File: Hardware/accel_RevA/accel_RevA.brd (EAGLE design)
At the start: 100 x 80 mm, 12 parts, among them U1 MMA8452Q

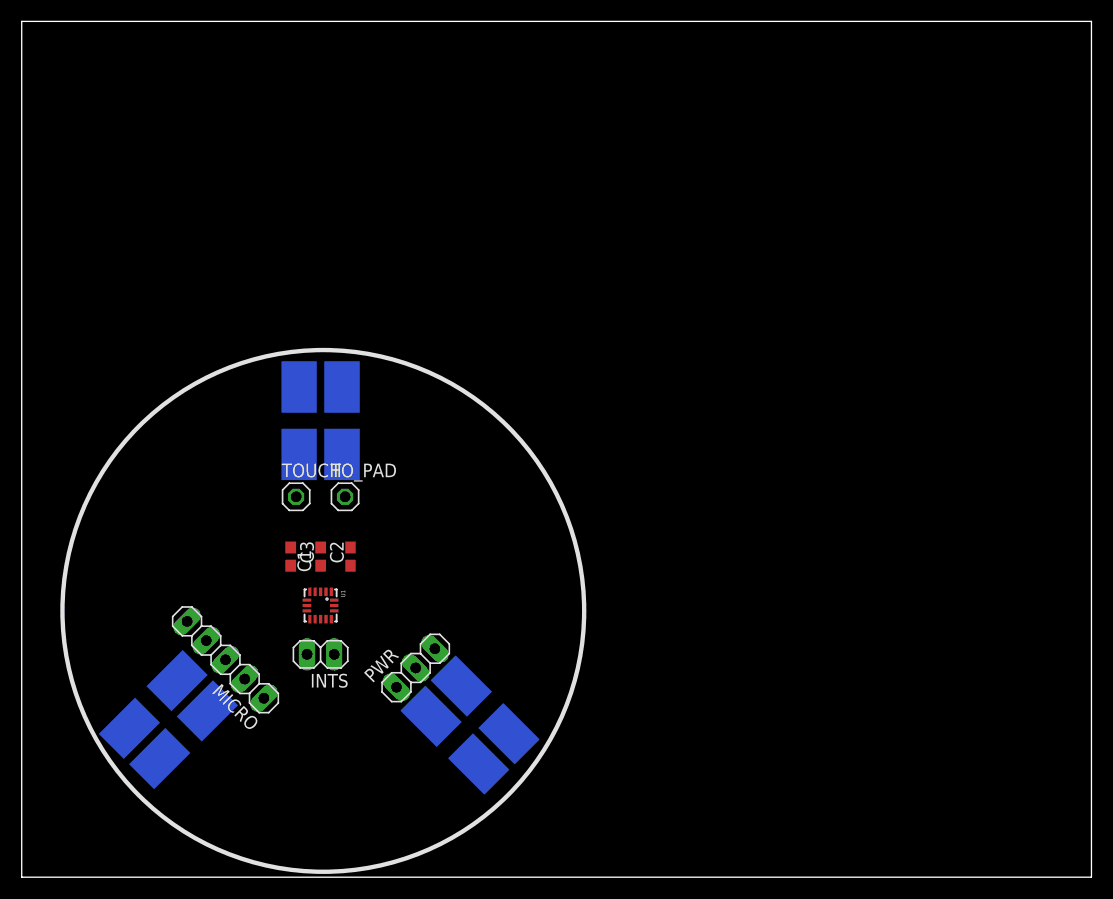
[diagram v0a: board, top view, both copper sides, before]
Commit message: Update of revA of accel board
Completed routing of board!! No rats nest left, passes DRC and ERC.
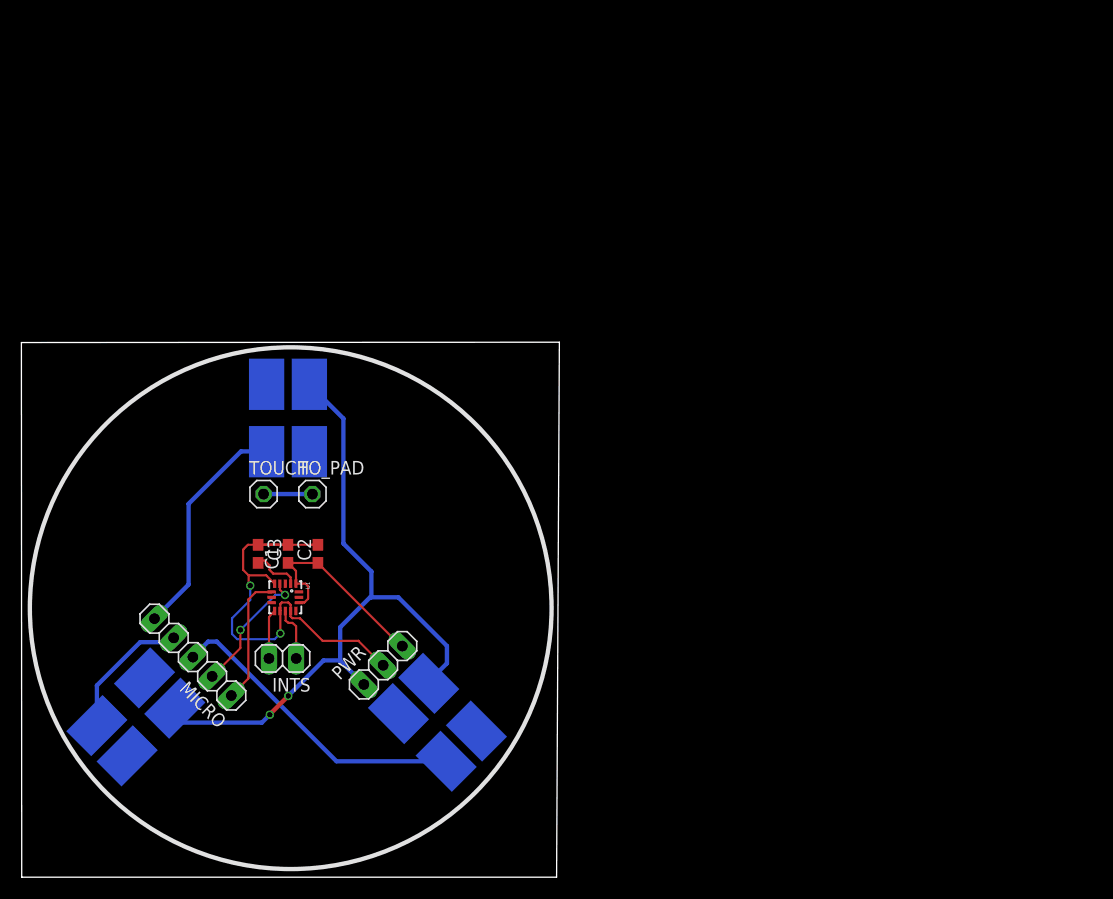
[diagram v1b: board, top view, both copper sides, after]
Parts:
- moved INTS 3.58 mm to (24.4, 20.4)
- moved U1 3.39 mm to (24.6, 26.2)
- moved LED3 3.06 mm to (24.9, 42.9)
- moved C1 3.06 mm to (22.1, 30.2)
- moved C2 3.06 mm to (27.7, 30.2)
- moved C3 3.06 mm to (24.9, 30.2)
- moved MICRO 3.06 mm to (16.0, 20.6)
- moved PWR 3.06 mm to (33.8, 19.8)
- moved LED2 3.06 mm to (10.7, 15.0)
- moved TOUCH 3.06 mm to (22.6, 35.8)
- moved TO_PAD 3.06 mm to (27.2, 35.8)
- moved LED1 3.06 mm to (38.9, 14.5)
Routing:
- net VDD: track 0.00 -> 65.1 mm, vias 0 -> 2
- net GND: track 0.00 -> 42.1 mm, vias 0 -> 2
- net LED1: track 0.00 -> 28.9 mm
- net LED3: track 0.00 -> 21.4 mm
- net VCC: track 0.00 -> 19.6 mm
- net LED2: track 0.00 -> 12.8 mm
- net SCL: track 0.00 -> 12.2 mm, vias 0 -> 2
- net SDA: track 0.00 -> 12.1 mm
- net N$1: track 0.00 -> 5.11 mm
- net N$2: track 0.00 -> 4.64 mm
- net N$3: track 0.00 -> 4.62 mm
- net TOUCH: track 0.00 -> 4.57 mm
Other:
- board size 100 x 80 mm -> 50.3 x 50 mm

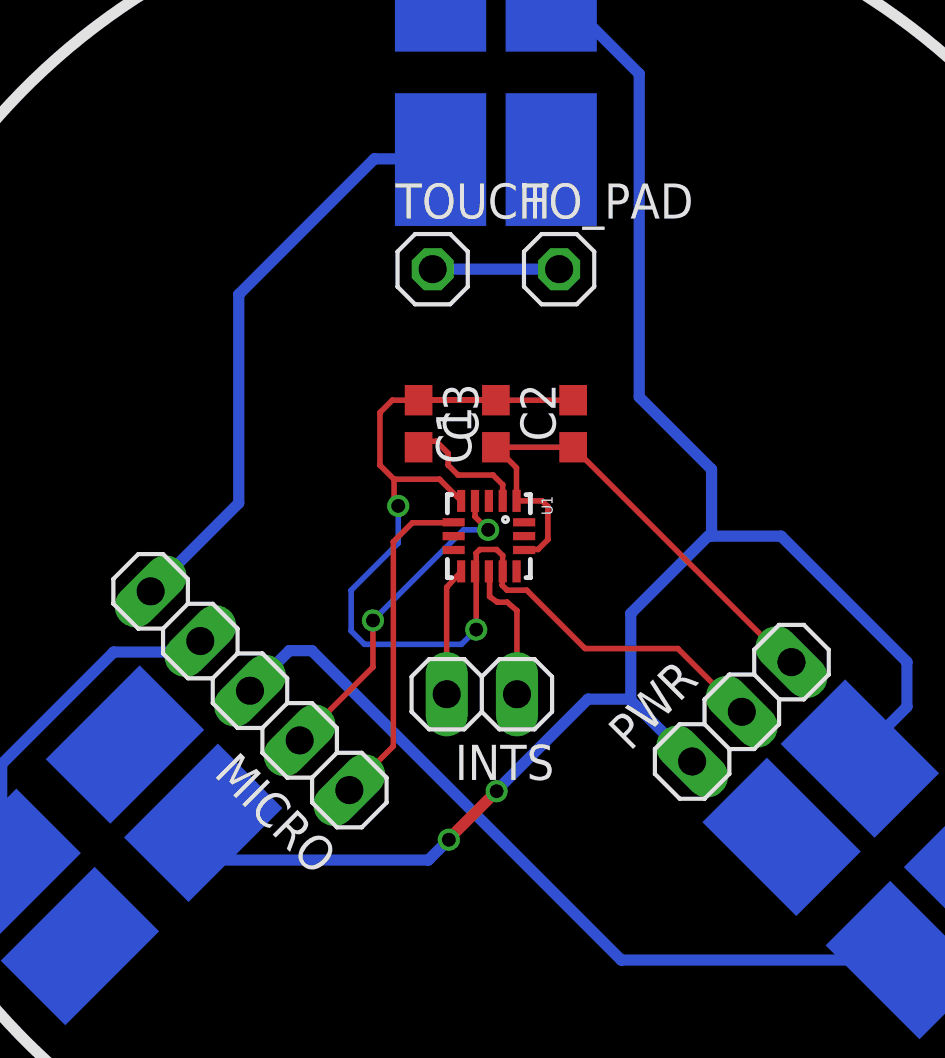
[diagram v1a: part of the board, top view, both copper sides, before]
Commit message: Added names to stuff on board
Just the names and stuff, not really much. Just needs some legit
artwork.
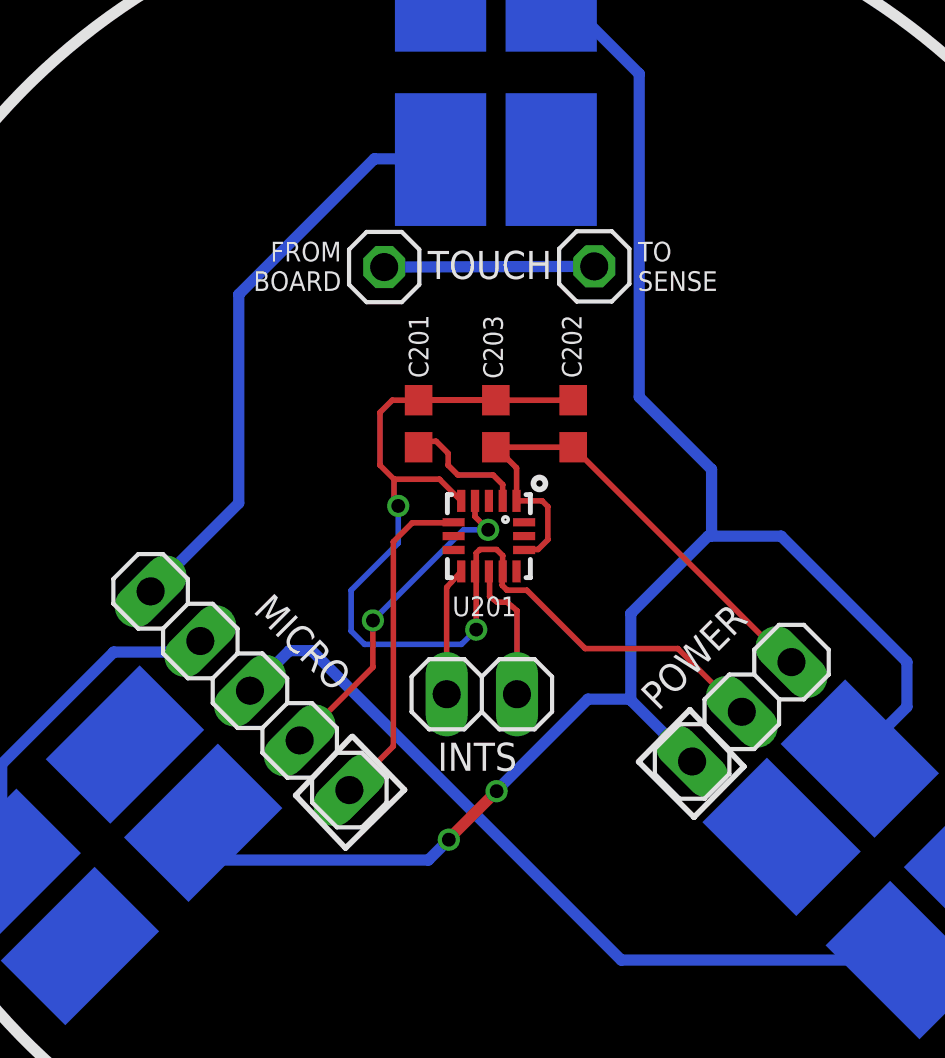
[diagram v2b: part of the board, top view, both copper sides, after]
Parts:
- moved TOUCH 1.75 mm to (20.9, 35.9)
- moved TO_PAD 1.27 mm to (28.4, 35.9)
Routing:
- net TOUCH: track 4.57 -> 7.59 mm
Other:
- board text added: "C201"
- board text added: "C202"
- board text added: "C203"
- board text added: "FROM BOARD"
- board text added: "INTS"
- board text added: "MICRO"
- board text added: "POWER"
- board text added: "TO SENSE"
- board text added: "TOUCH"
- board text added: "U201"
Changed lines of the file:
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@@
 <circle x="25.146" y="25.146" radius="24.385321875" width="0.4064" layer="21"/>
 <circle x="25.146" y="25.146" radius="24.385321875" width="0.4064" layer="22"/>
+<text x="22.4536" y="31.877" size="0.7112" layer="21" ratio="10" rot="R90">C201</text>
+<text x="25.146" y="31.8516" size="0.7112" layer="21" ratio="10" rot="R90">C203</text>
+<text x="27.9908" y="31.877" size="0.7112" layer="21" ratio="10" rot="R90">C202</text>
+<circle x="26.4668" y="28.067" radius="0.217015625" width="0.2032" layer="21"/>
+<text x="23.3172" y="23.2664" size="0.7112" layer="21" ratio="10">U201</text>
+<text x="22.7838" y="17.6784" size="1.016" layer="21" ratio="16">INTS</text>
+<text x="16.0782" y="23.4442" size="1.016" layer="21" ratio="16" rot="R315">MICRO</text>
+<text x="30.7594" y="19.812" size="1.016" layer="21" ratio="16" rot="R45">POWER</text>
+<text x="22.4282" y="35.4584" size="1.016" layer="21" ratio="19">TOUCH</text>
+<wire x1="19.7104" y1="18.923" x2="21.59" y2="16.9926" width="0.2032" layer="21"/>
+<wire x1="21.59" y1="16.9926" x2="19.4564" y2="14.8844" width="0.2032" layer="21"/>
+<wire x1="19.4564" y1="14.8844" x2="17.653" y2="16.7894" width="0.2032" layer="21"/>
+<wire x1="17.653" y1="16.7894" x2="19.6596" y2="18.8976" width="0.2032" layer="21"/>
+<wire x1="30.0482" y1="18.0086" x2="31.9024" y2="19.8882" width="0.2032" layer="21"/>
+<wire x1="31.9024" y1="19.8882" x2="33.8582" y2="17.8308" width="0.2032" layer="21"/>
+<wire x1="33.8582" y1="17.8308" x2="32.0548" y2="16.002" width="0.2032" layer="21"/>
+<wire x1="32.0548" y1="16.002" x2="30.0736" y2="17.9832" width="0.2032" layer="21"/>
+<text x="30.0228" y="35.0266" size="0.7112" layer="21">TO
+SENSE</text>
+<text x="19.304" y="35.0266" size="0.7112" layer="21" align="bottom-right">FROM
+BOARD</text>
 </plain>
 <attributes>
@@
 </autorouter>
 <elements>
-<element name="U1" library="SparkFun-Sensors" package="QFN-16_0.5MM" value="MMA8452Q" x="24.638" y="26.162" rot="R270">
+<element name="U1" library="SparkFun-Sensors" package="QFN-16_0.5MM" value="MMA8452Q" x="24.638" y="26.162" smashed="yes" rot="R270">
 <attribute name="PROD_ID" value="IC-10769" x="-2.032" y="2.032" size="1.778" layer="27" rot="R270" display="off"/>
-</element>
-<element name="C1" library="eagle-ltspice" package="C0603" value="0.1u" x="22.098" y="30.226" rot="R270">
+<attribute name="VALUE" x="22.2746" y="27.6136" size="0.4064" layer="27" rot="R270"/>
+</element>
+<element name="C1" library="eagle-ltspice" package="C0603" value="0.1u" x="22.098" y="30.226" smashed="yes" rot="R270">
 <attribute name="SPICEMODEL" value="NONE" x="-9.652" y="13.716" size="1.778" layer="27" rot="R270" display="off"/>
 <attribute name="SPICEPREFIX" value="C" x="-9.652" y="13.716" size="1.778" layer="27" rot="R270" display="off"/>
-</element>
-<element name="C2" library="eagle-ltspice" package="C0603" value="0.1u" x="27.686" y="30.226" rot="R90">
+<attribute name="VALUE" x="20.193" y="30.861" size="1.27" layer="27" rot="R270"/>
+</element>
+<element name="C2" library="eagle-ltspice" package="C0603" value="0.1u" x="27.686" y="30.226" smashed="yes" rot="R90">
 <attribute name="SPICEMODEL" value="NONE" x="59.436" y="51.816" size="1.778" layer="27" rot="R90" display="off"/>
 <attribute name="SPICEPREFIX" value="C" x="59.436" y="51.816" size="1.778" layer="27" rot="R90" display="off"/>
-</element>
-<element name="PWR" library="pinhead" package="1X03" value="" x="33.782" y="19.812" rot="R45"/>
-<element name="MICRO" library="pinhead" package="1X05" value="" x="16.002" y="20.574" rot="R135"/>
-<element name="C3" library="eagle-ltspice" package="C0603" value="4.7u" x="24.892" y="30.226" rot="R90">
+<attribute name="VALUE" x="29.591" y="29.591" size="1.27" layer="27" rot="R90"/>
+</element>
+<element name="PWR" library="pinhead" package="1X03" value="" x="33.782" y="19.812" smashed="yes" rot="R45">
+<attribute name="VALUE" x="33.332984375" y="14.87285625" size="1.27" layer="27" rot="R45"/>
+</element>
+<element name="MICRO" library="pinhead" package="1X05" value="" x="16.002" y="20.574" smashed="yes" rot="R135">
+<attribute name="VALUE" x="22.737190625" y="18.328934375" size="1.27" layer="27" rot="R135"/>
+</element>
+<element name="C3" library="eagle-ltspice" package="C0603" value="4.7u" x="24.892" y="30.226" smashed="yes" rot="R90">
 <attribute name="SPICEMODEL" value="NONE" x="56.642" y="56.896" size="1.778" layer="27" rot="R90" display="off"/>
 <attribute name="SPICEPREFIX" value="C" x="56.642" y="56.896" size="1.778" layer="27" rot="R90" display="off"/>
-</element>
-<element name="TOUCH" library="pinhead" package="1X01" value="" x="22.606" y="35.814"/>
-<element name="TO_PAD" library="pinhead" package="1X01" value="" x="27.178" y="35.814"/>
-<element name="LED1" library="led" package="P-LCC-4" value="" x="38.862" y="14.478" rot="MR315"/>
-<element name="LED2" library="led" package="P-LCC-4" value="" x="10.668" y="14.986" rot="MR45"/>
-<element name="LED3" library="led" package="P-LCC-4" value="" x="24.892" y="42.926" rot="MR0"/>
-<element name="INTS" library="pinhead" package="1X02" value="" x="24.384" y="20.447" rot="R180"/>
+<attribute name="VALUE" x="26.797" y="29.591" size="1.27" layer="27" rot="R90"/>
+</element>
+<element name="TOUCH" library="pinhead" package="1X01" value="" x="20.8534" y="35.8902" smashed="yes">
+<attribute name="VALUE" x="19.5834" y="32.7152" size="1.27" layer="27"/>
+</element>
+<element name="TO_PAD" library="pinhead" package="1X01" value="" x="28.448" y="35.9156" smashed="yes">
+<attribute name="VALUE" x="27.178" y="32.7406" size="1.27" layer="27"/>
+</element>
+<element name="LED1" library="led" package="P-LCC-4" value="" x="38.862" y="14.478" smashed="yes" rot="MR315">
+<attribute name="VALUE" x="37.06595" y="9.08984375" size="1.27" layer="28" rot="MR45"/>
+</element>
+<element name="LED2" library="led" package="P-LCC-4" value="" x="10.668" y="14.986" smashed="yes" rot="MR45">
+<attribute name="VALUE" x="5.279846875" y="16.78205" size="1.27" layer="28" rot="MR135"/>
+</element>
+<element name="LED3" library="led" package="P-LCC-4" value="" x="24.892" y="42.926" smashed="yes" rot="MR0">
+<attribute name="VALUE" x="19.812" y="40.386" size="1.27" layer="28" rot="MR90"/>
+</element>
+<element name="INTS" library="pinhead" package="1X02" value="" x="24.384" y="20.447" smashed="yes" rot="R180">
+<attribute name="VALUE" x="26.924" y="23.622" size="1.27" layer="27" rot="R180"/>
+</element>
 </elements>
 <signals>
@@
 <contactref element="TOUCH" pad="1"/>
 <contactref element="TO_PAD" pad="1"/>
-<wire x1="22.606" y1="35.814" x2="27.178" y2="35.814" width="0.4064" layer="16"/>
+<wire x1="20.8534" y1="35.8902" x2="28.448" y2="35.9156" width="0.4064" layer="16"/>
 </signal>
 <signal name="N$1">
@@
 </board>
 </drawing>
+<compatibility>
+<note version="6.3" minversion="6.2.2" severity="warning">
+Since Version 6.2.2 text objects can contain more than one line,
+which will not be processed correctly with this version.
+</note>
+</compatibility>
 </eagle>

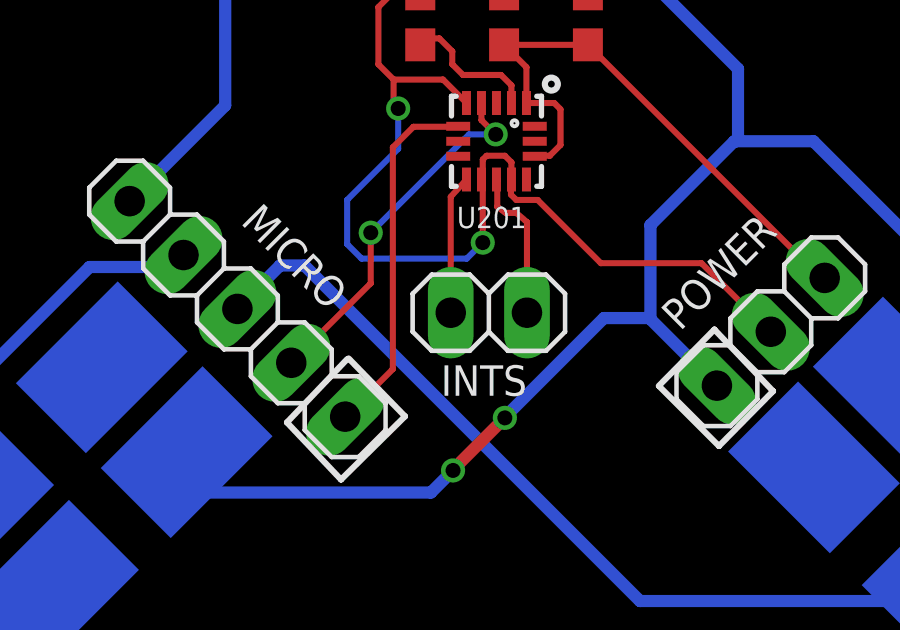
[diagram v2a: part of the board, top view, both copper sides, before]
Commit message: Finished micro and adjusted text of accel
MUST CHECK THAT TPLACE IS ON SILSCREEN OR SHIT!!!
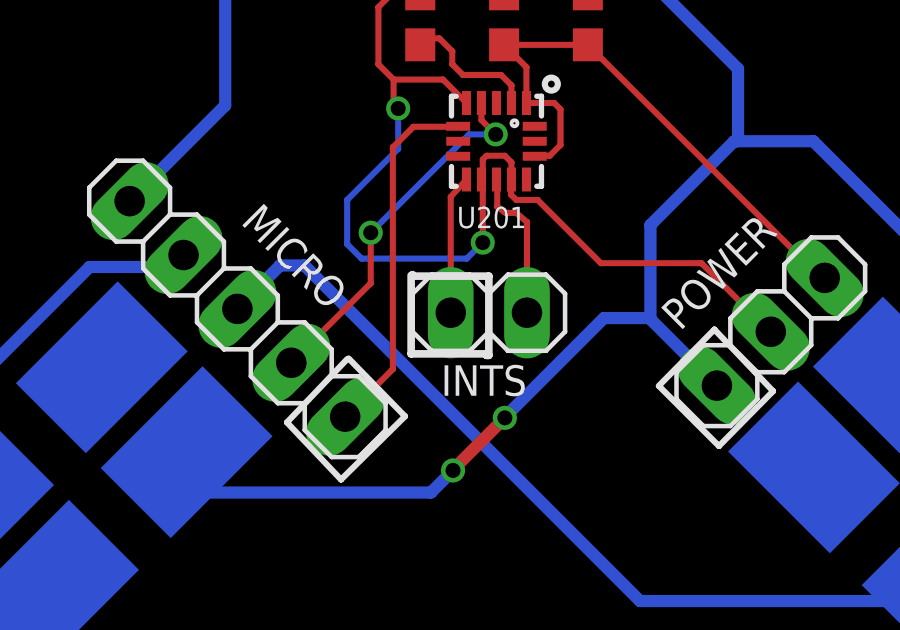
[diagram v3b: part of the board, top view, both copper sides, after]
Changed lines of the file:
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@@
 <layer number="25" name="tNames" color="15" fill="1" visible="yes" active="yes"/>
 <layer number="26" name="bNames" color="15" fill="1" visible="yes" active="yes"/>
-<layer number="27" name="tValues" color="7" fill="1" visible="no" active="yes"/>
-<layer number="28" name="bValues" color="7" fill="1" visible="no" active="yes"/>
+<layer number="27" name="tValues" color="7" fill="1" visible="yes" active="yes"/>
+<layer number="28" name="bValues" color="7" fill="1" visible="yes" active="yes"/>
 <layer number="29" name="tStop" color="7" fill="3" visible="yes" active="yes"/>
 <layer number="30" name="bStop" color="7" fill="6" visible="yes" active="yes"/>
@@
 <layer number="50" name="dxf" color="7" fill="1" visible="no" active="no"/>
 <layer number="51" name="tDocu" color="6" fill="1" visible="yes" active="yes"/>
-<layer number="52" name="bDocu" color="7" fill="1" visible="yes" active="yes"/>
+<layer number="52" name="bDocu" color="6" fill="1" visible="yes" active="yes"/>
 <layer number="53" name="tGND_GNDA" color="7" fill="9" visible="no" active="no"/>
 <layer number="54" name="bGND_GNDA" color="1" fill="9" visible="no" active="no"/>
@@
 <text x="19.304" y="35.0266" size="0.7112" layer="21" align="bottom-right">FROM
 BOARD</text>
+<wire x1="21.7932" y1="21.6916" x2="21.7932" y2="19.0754" width="0.254" layer="21"/>
+<wire x1="21.7932" y1="19.0754" x2="24.3078" y2="19.0754" width="0.254" layer="21"/>
+<wire x1="24.3078" y1="19.0754" x2="24.3078" y2="19.0246" width="0.254" layer="21"/>
+<wire x1="24.3078" y1="19.0246" x2="24.384" y2="19.0246" width="0.254" layer="21"/>
+<wire x1="24.384" y1="19.0246" x2="24.384" y2="21.6662" width="0.254" layer="21"/>
+<wire x1="24.384" y1="21.6662" x2="21.844" y2="21.6662" width="0.254" layer="21"/>
+<wire x1="21.844" y1="21.6662" x2="21.844" y2="21.717" width="0.254" layer="21"/>
 </plain>
 <attributes>
@@
 <element name="U1" library="SparkFun-Sensors" package="QFN-16_0.5MM" value="MMA8452Q" x="24.638" y="26.162" smashed="yes" rot="R270">
 <attribute name="PROD_ID" value="IC-10769" x="-2.032" y="2.032" size="1.778" layer="27" rot="R270" display="off"/>
-<attribute name="VALUE" x="22.2746" y="27.6136" size="0.4064" layer="27" rot="R270"/>
 </element>
 <element name="C1" library="eagle-ltspice" package="C0603" value="0.1u" x="22.098" y="30.226" smashed="yes" rot="R270">
 <attribute name="SPICEMODEL" value="NONE" x="-9.652" y="13.716" size="1.778" layer="27" rot="R270" display="off"/>
 <attribute name="SPICEPREFIX" value="C" x="-9.652" y="13.716" size="1.778" layer="27" rot="R270" display="off"/>
-<attribute name="VALUE" x="20.193" y="30.861" size="1.27" layer="27" rot="R270"/>
 </element>
 <element name="C2" library="eagle-ltspice" package="C0603" value="0.1u" x="27.686" y="30.226" smashed="yes" rot="R90">
 <attribute name="SPICEMODEL" value="NONE" x="59.436" y="51.816" size="1.778" layer="27" rot="R90" display="off"/>
 <attribute name="SPICEPREFIX" value="C" x="59.436" y="51.816" size="1.778" layer="27" rot="R90" display="off"/>
-<attribute name="VALUE" x="29.591" y="29.591" size="1.27" layer="27" rot="R90"/>
 </element>
 <element name="PWR" library="pinhead" package="1X03" value="" x="33.782" y="19.812" smashed="yes" rot="R45">
@@
 <attribute name="SPICEMODEL" value="NONE" x="56.642" y="56.896" size="1.778" layer="27" rot="R90" display="off"/>
 <attribute name="SPICEPREFIX" value="C" x="56.642" y="56.896" size="1.778" layer="27" rot="R90" display="off"/>
-<attribute name="VALUE" x="26.797" y="29.591" size="1.27" layer="27" rot="R90"/>
 </element>
 <element name="TOUCH" library="pinhead" package="1X01" value="" x="20.8534" y="35.8902" smashed="yes">
